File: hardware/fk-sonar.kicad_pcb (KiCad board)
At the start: 2 copper layers, 28.4 x 70.3 mm, 77 parts, among them J1 Conn_01x03, J2 CONN-HDR-2x5, J3 RF-SMA-EDGE, J4 MICRO-USB, J5 S2B-PH-SM4-TB, J6 Conn_01x04, J7 S2B-PH-SM4-TB, J8 Conn_01x01, J9 Conn_01x01, Q1 2N7002LT1G, Q2 2N7002LT1G, Q3 2N7002LT1G, Q4 2N7002LT1G, SW1 SPNO, U1 ATSAMD21G18A-AU, U2 RFM95W, U3 BQ24074RGTT, U4 S25FL116K0XMFI041, U5 MAX1704XX, U6 MCP1700T-3302E/MB, Y1 FC-135

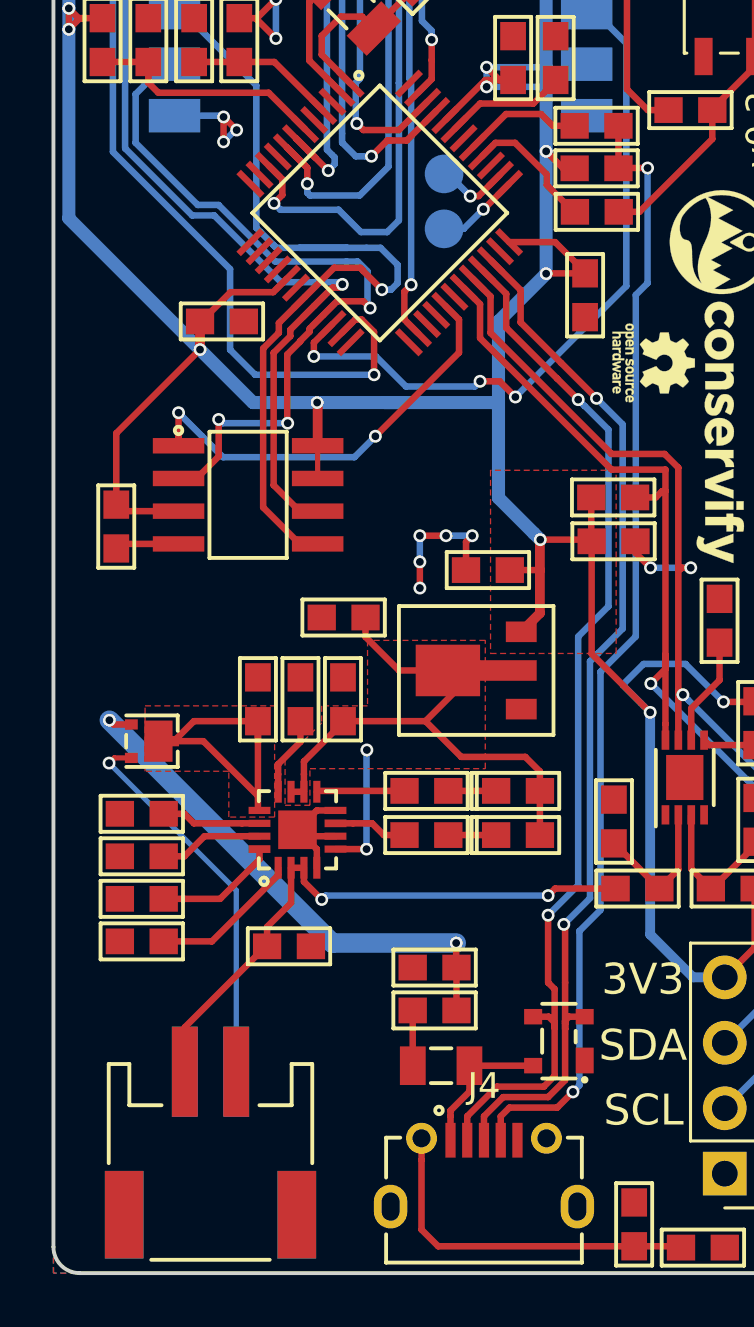
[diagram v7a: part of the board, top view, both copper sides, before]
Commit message: Fix USB footprint. Add a Molex for D30/D31 serial.
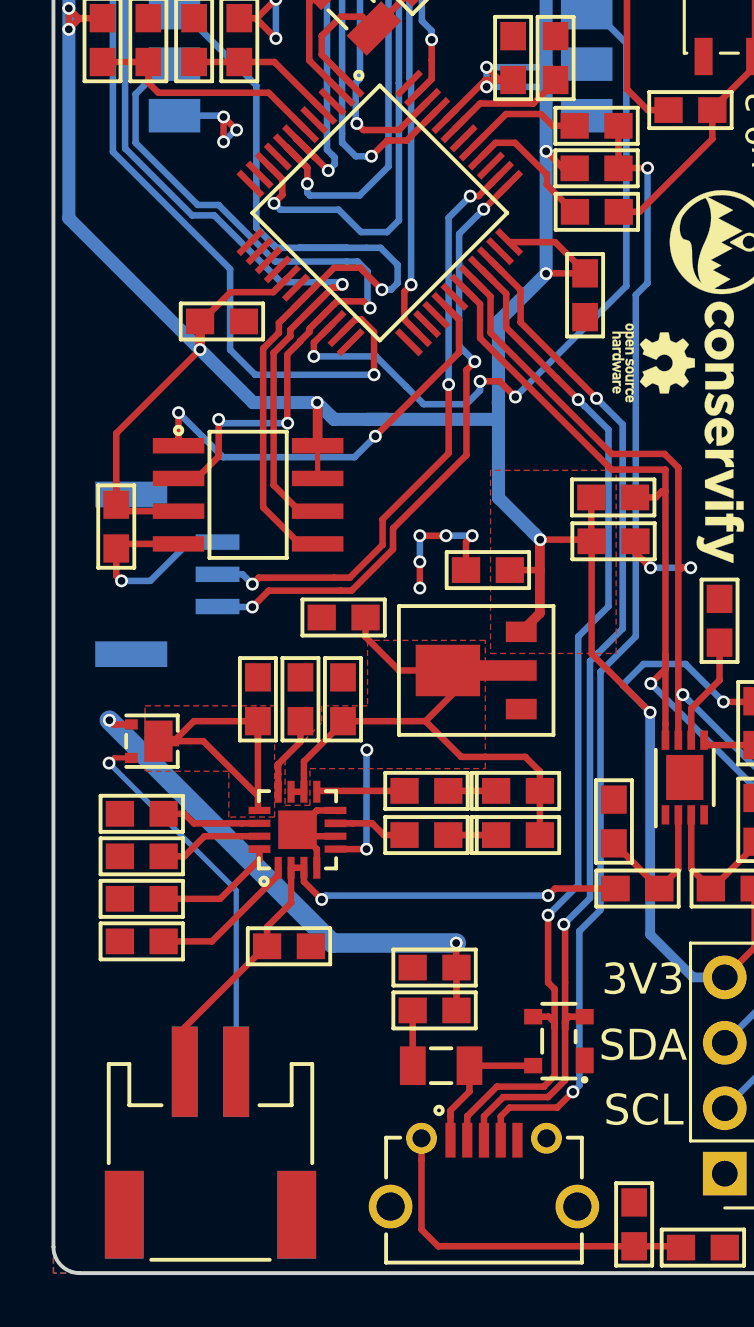
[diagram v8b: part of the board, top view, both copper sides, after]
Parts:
- removed J9: Conn_01x01, Measurement_Points:Measurement_Point_Round-SMD-Pad_Small
- J4: footprint RocketScreamKicadLibrary:MICRO-USB -> conservify:MICRO-USB
- J8: value Conn_01x01 -> Conn_01x03; footprint Measurement_Points:Measurement_Point_Round-SMD-Pad_Small -> conservify:Molex_CLIK-Mate_502382-0370_1x03_P1.25mm_Vertical
- moved J8 18.9 mm to (129.7, 105.4), turned to 270 degrees
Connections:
- J8 pad 1: /D31 -> GND
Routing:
- net /D30: track 3.25 -> 24.3 mm, vias 1 -> 3
- net /D31: track 2.87 -> 23.6 mm, vias 1 -> 3
- net GND: track 27.6 -> 33.3 mm, vias 13 -> 14
- net /RADIO_D0: track 27.7 -> 28.5 mm
